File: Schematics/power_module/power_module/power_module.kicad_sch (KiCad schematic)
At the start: 10 parts, among them J1 Stack Female Edge Connector, U1 ID_LM66100DCKR, U2 ID_LM66100DCKR

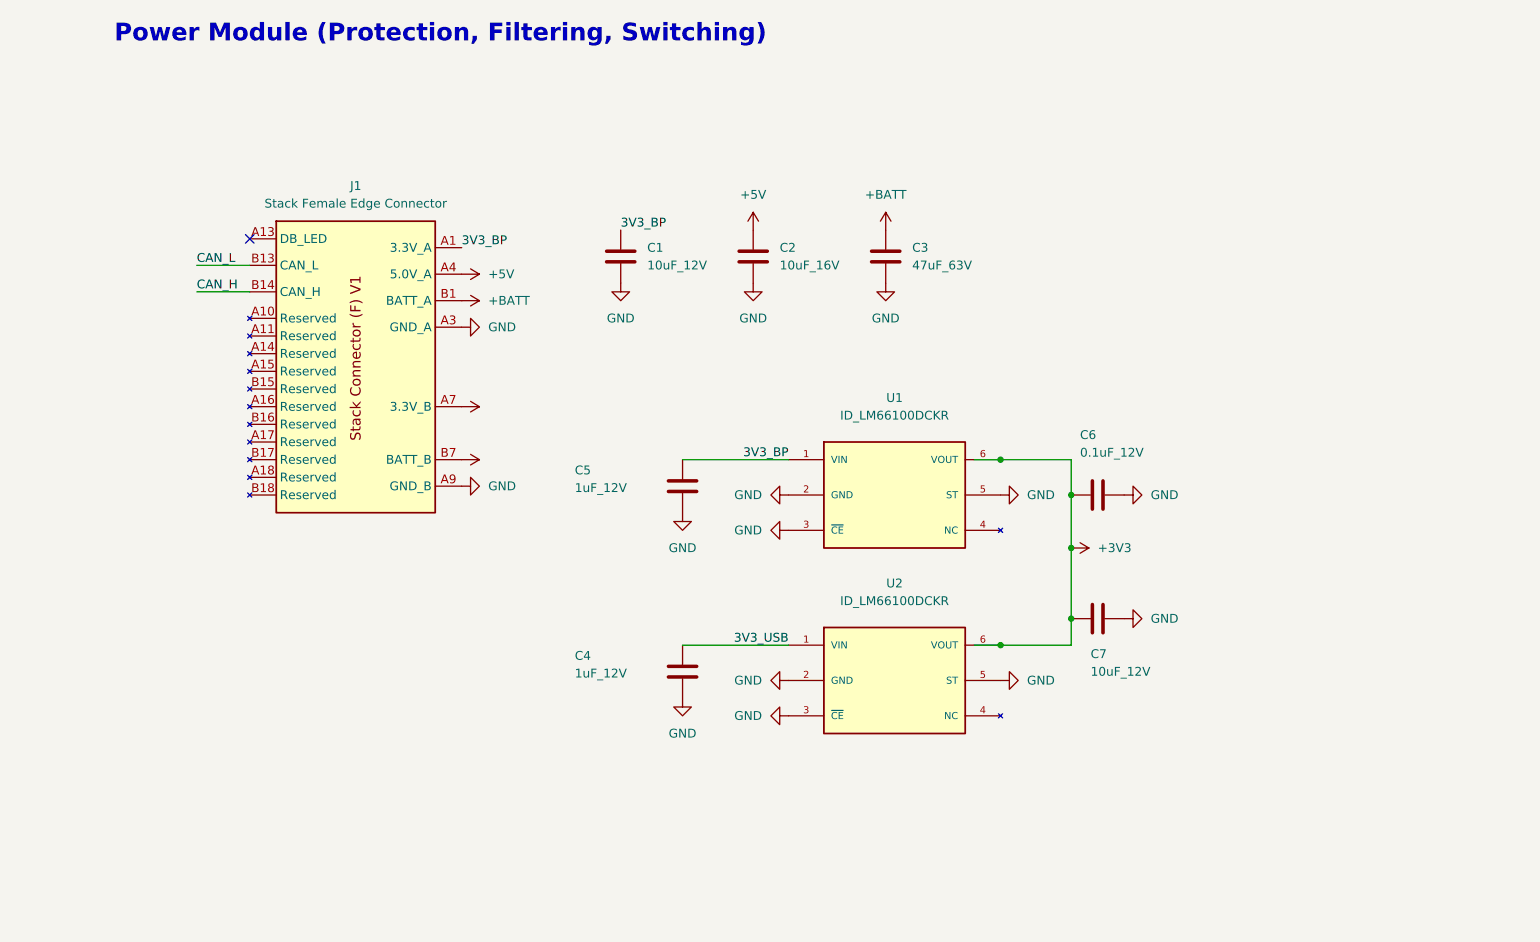
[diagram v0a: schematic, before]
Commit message: add power module with ORing circuit, add datasheets on each symbol.
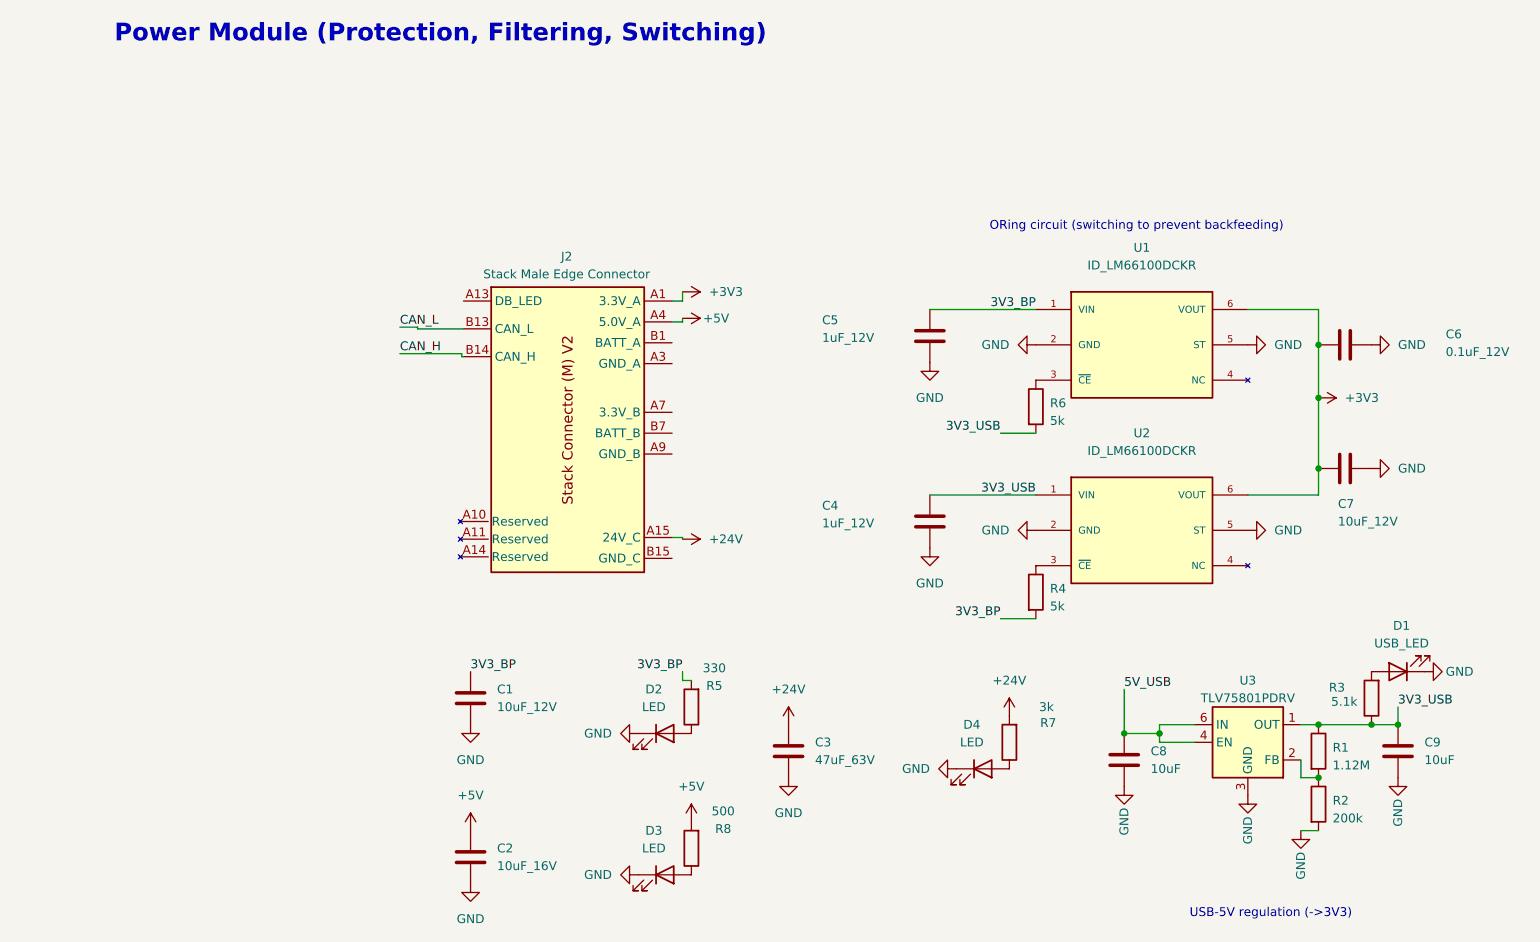
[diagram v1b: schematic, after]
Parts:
- removed J1: Stack Female Edge Connector, footprints:AMPHENOL_10018784-10210TLF, symbol EdgeConnector:Stack Female Edge Connector
- added C8, C9: 10uF, Capacitor_SMD:C_0603_1608Metric, symbol Device:C
- added D1: USB_LED, LED_SMD:LED_0603_1608Metric, symbol Device:LED
- added D2, D3, D4: LED, symbol Device:LED
- added J2: Stack Male Edge Connector, Connector_PCBEdge:BUS_PCIexpress_x1, symbol EdgeConnector:Stack Male Edge Connector
- added R1: 1.12M, Resistor_SMD:R_0603_1608Metric, symbol Device:R
- added R2: 200k, Resistor_SMD:R_0603_1608Metric, symbol Device:R
- added R3: 5.1k, Resistor_SMD:R_0603_1608Metric, symbol Device:R
- added R4, R6: 5k, Resistor_SMD:R_0603_1608Metric, symbol Device:R
- added R5: 330, symbol Device:R
- added R7: 3k, symbol Device:R
- added R8: 500, symbol Device:R
- added U3: TLV75801PDRV, Package_SON:WSON-6-1EP_2x2mm_P0.65mm_EP1x1.6mm, symbol Regulator_Linear:TLV75801PDRV
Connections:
- net +3V3: now also J2.A1 (3.3V_A), J2.A2 (3.3V_A)
- net +5V: now also J2.A4 (5.0V_A), J2.A5 (5.0V_A), R8.2
- net 3V3_BP: now also R4.2, R5.2
- net 3V3_USB: now also C9.1, R1.1, R3.1, R6.2, U3.1 (OUT)
- net CAN_H: now also J2.B14 (CAN_H)
- net CAN_L: now also J2.B13 (CAN_L)
- net GND: now also C8.2, C9.2, D1.1 (K), D2.1 (K), D3.1 (K), D4.1 (K), R2.2, U3.3 (GND), U3.7 (GND); no longer U1.3 (~{CE}), U2.3 (~{CE})
- net +BATT renamed +24V
- net +24V: now also J2.A15 (24V_C), J2.A16 (24V_C), J2.A17 (24V_C), J2.A18 (24V_C), R7.2
- new net: R1.2, R2.1, U3.2 (FB)
- new net: D1.2 (A), R3.2
- new net: D4.2 (A), R7.1
- new net: R6.1, U1.3 (~{CE})
- new net: D3.2 (A), R8.1
- new net: R4.1, U2.3 (~{CE})
- new net: D2.2 (A), R5.1
- new net: J2.A12 (GND_B), J2.A9 (GND_B), J2.B10 (GND_B), J2.B11 (GND_B), J2.B12 (GND_B)
- new net: J2.A3 (GND_A), J2.A6 (GND_A), J2.B4 (GND_A), J2.B5 (GND_A), J2.B6 (GND_A)
- new net: J2.A7 (3.3V_B), J2.A8 (3.3V_B)
- new net: J2.B1 (BATT_A), J2.B2 (BATT_A), J2.B3 (BATT_A)
- new net: J2.B15 (GND_C), J2.B16 (GND_C), J2.B17 (GND_C), J2.B18 (GND_C)
- new net: J2.B7 (BATT_B), J2.B8 (BATT_B), J2.B9 (BATT_B)
- new net 5V_USB: C8.1, U3.4 (EN), U3.6 (IN)
- no-connect marks 1 -> 0
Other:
- note added: "ORing circuit (switching to prevent backfeeding)"
- note added: "USB-5V regulation (->3V3)"
- moved on the sheet: C1, C2, C3, C4, C5, C6, C7, U1, U2

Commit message: update power module
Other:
- note added: "Power Circuitry (Protection, Filtering, Switching)"
- note removed: "Power Module (Protection, Filtering, Switching)"
- title: ULC Board Power Module -> ULC Board Power Circuitry
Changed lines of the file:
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@@
 	(paper "A4")
 	(title_block
-		(title "ULC Board Power Module")
+		(title "ULC Board Power Circuitry")
 		(rev "A")
 		(company "Queen's Rocket Engineering Team")
+		(comment 1 "Jeevan Sanchez")
 	)
 	(junction
@@
 		)
 	)
-	(text "Power Module (Protection, Filtering, Switching)\n"
+	(text "Power Circuitry (Protection, Filtering, Switching)\n"
 		(exclude_from_sim no)
 		(at 61.722 18.796 0)

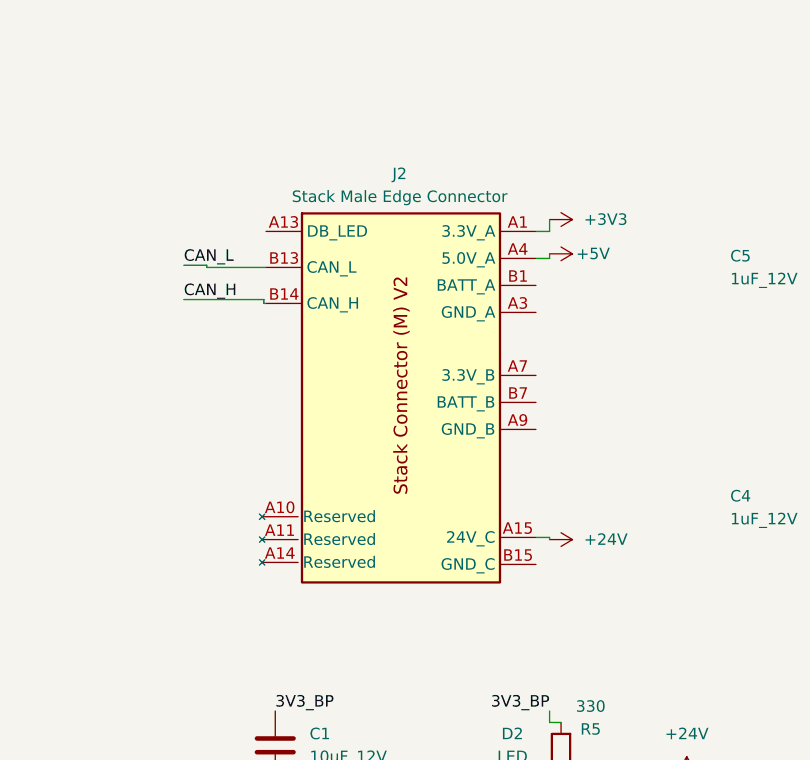
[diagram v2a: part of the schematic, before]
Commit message: update power circuitry with new backplane symbol
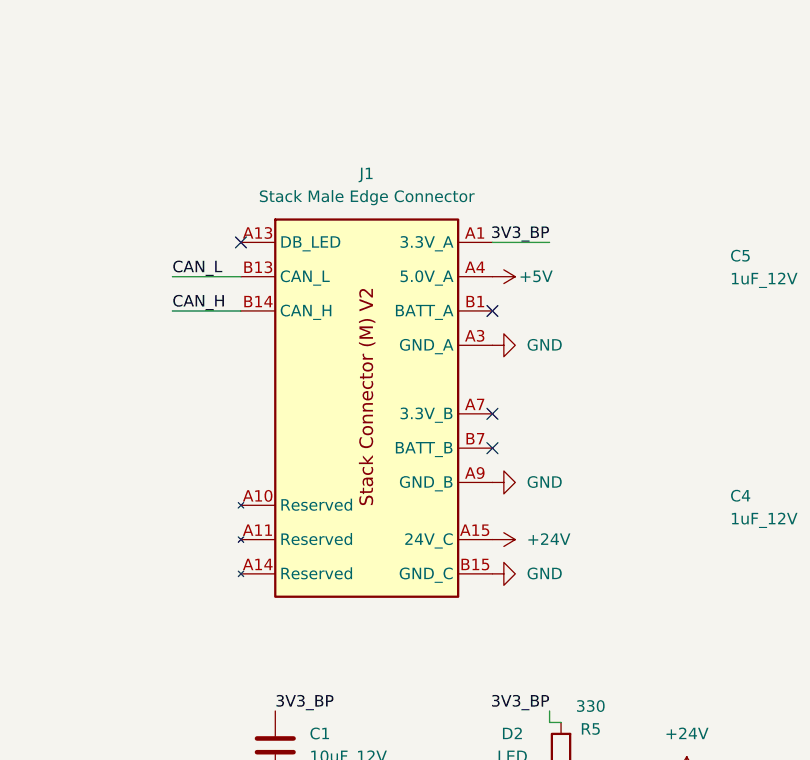
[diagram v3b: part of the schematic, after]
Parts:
- removed J2: Stack Male Edge Connector, Connector_PCBEdge:BUS_PCIexpress_x1, symbol EdgeConnector:Stack Male Edge Connector
- added J1: Stack Male Edge Connector, Connector_PCBEdge:BUS_PCIexpress_x1, symbol EdgeConnector:Stack Male Edge Connector
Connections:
- net +24V: now also J1.A15 (24V_C), J1.A16 (24V_C), J1.A17 (24V_C), J1.A18 (24V_C)
- net +5V: now also J1.A4 (5.0V_A), J1.A5 (5.0V_A)
- net 3V3_BP: now also J1.A1 (3.3V_A), J1.A2 (3.3V_A)
- net CAN_H: now also J1.B14 (CAN_H)
- net CAN_L: now also J1.B13 (CAN_L)
- net GND: now also J1.A12 (GND_B), J1.A3 (GND_A), J1.A6 (GND_A), J1.A9 (GND_B), J1.B10 (GND_B), J1.B11 (GND_B), J1.B12 (GND_B), J1.B15 (GND_C), J1.B16 (GND_C), J1.B17 (GND_C), J1.B18 (GND_C), J1.B4 (GND_A), J1.B5 (GND_A), J1.B6 (GND_A)
- new net: J1.A7 (3.3V_B), J1.A8 (3.3V_B)
- new net: J1.B1 (BATT_A), J1.B2 (BATT_A), J1.B3 (BATT_A)
- new net: J1.B7 (BATT_B), J1.B8 (BATT_B), J1.B9 (BATT_B)
- no-connect marks 0 -> 4
